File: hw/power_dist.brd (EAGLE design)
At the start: 80 x 50 mm, 87 parts, among them J1 JST-ZH6SMT_VERT, J2 JST-PH4SMT_VERT, J3 JST-PH5VERT, P1 XT30P, P2 XT30P, P3 XT30P, P4 XT30P, P5 XT30P, P6 XT30P, P7 XT90PW-M, Q1 PSMN4R8-100BSEJ, Q2 PSMN4R8-100BSEJ, Q3 PSMN4R8-100BSEJ, Q4 MF-DSC-SOT233-MMBT3904, Q5 MMBT5401 100V, U1 MAX15062AATA+T, U2 STM32G474CEU6, U3 TPS2490DGSR, U4 TCAN334G, U5 LT1787HVIMS8PBF, U6 STLM20DD9FUDFN-4L_STM-L

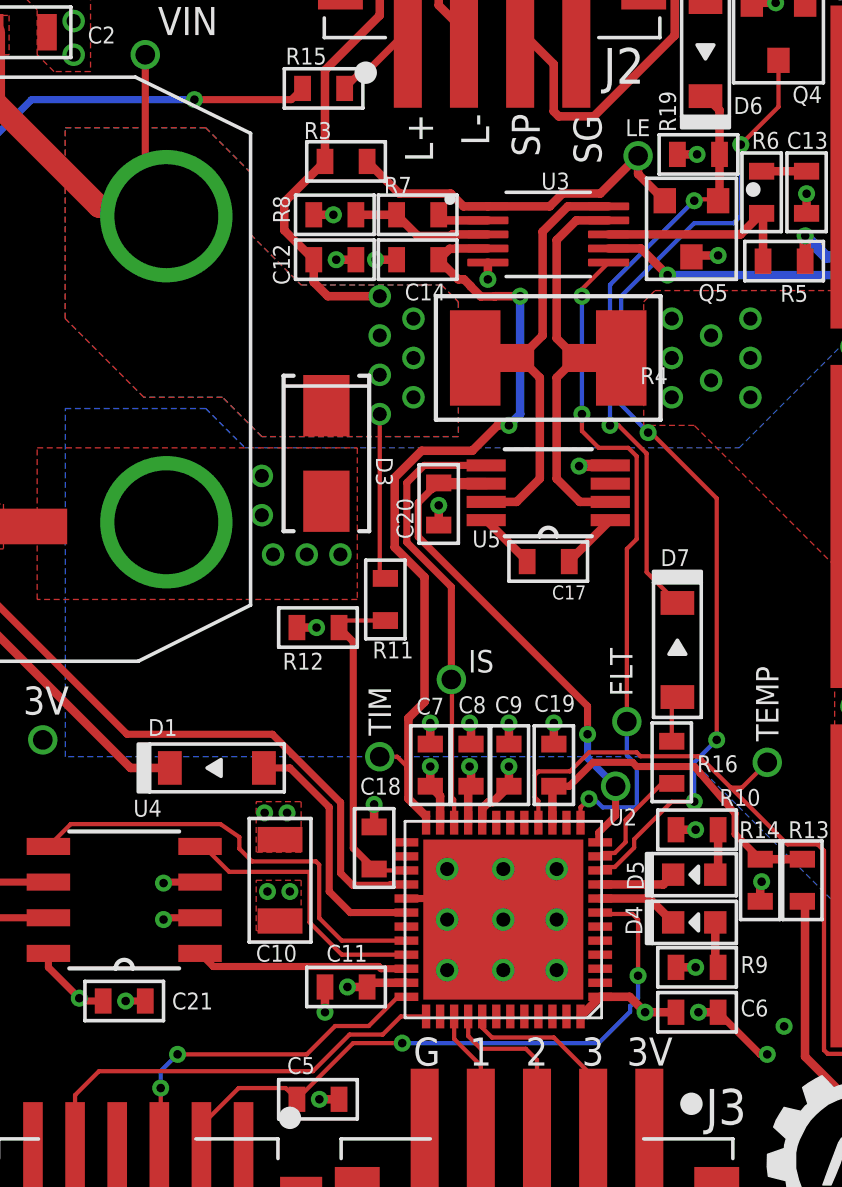
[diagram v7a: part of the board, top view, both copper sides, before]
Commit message: Update version pins for r4.2
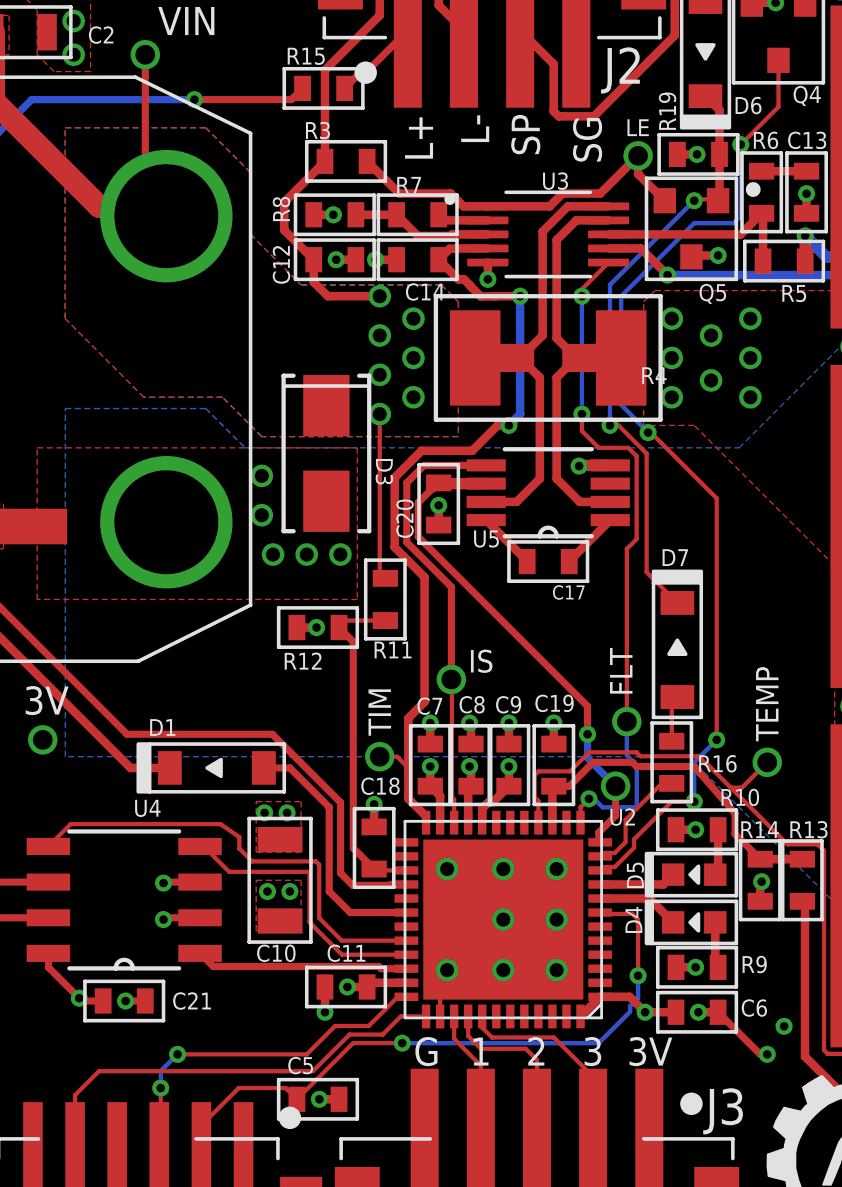
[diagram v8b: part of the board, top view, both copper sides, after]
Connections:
- net GND: now also U2.38; no longer U2.29
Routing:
- net GND: track 64.6 -> 64.5 mm, vias 51 -> 50
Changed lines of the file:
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@@
 <attribute name="HOUSEPART" value="1" x="32.35" y="38.3" size="1.778" layer="27" display="off"/>
 <attribute name="MPN" value="" x="32.35" y="38.3" size="1.778" layer="27" display="off"/>
-<attribute name="NAME" x="31.15" y="39.05" size="0.6" layer="25" font="vector" ratio="10"/>
+<attribute name="NAME" x="31.55" y="39.05" size="0.6" layer="25" font="vector" ratio="10"/>
 <attribute name="POPULATE" value="1" x="32.35" y="38.3" size="1.778" layer="27" display="off"/>
 <attribute name="TOLERANCE" value="" x="32.35" y="38.3" size="1.778" layer="27" display="off"/>
@@
 <contactref element="C2" pad="P$2"/>
 <contactref element="J3" pad="5"/>
-<contactref element="U2" pad="29"/>
 <contactref element="DB_G" pad="P$1"/>
 <via x="20.1" y="45.2" extent="1-16" drill="0.5"/>
@@
 <via x="35.4" y="15" extent="1-16" drill="0.5"/>
 <via x="37.3" y="15" extent="1-16" drill="0.5"/>
-<via x="33.4" y="13.2" extent="1-16" drill="0.5"/>
 <via x="35.4" y="13.2" extent="1-16" drill="0.5"/>
 <via x="37.3" y="13.2" extent="1-16" drill="0.5"/>
@@
 <via x="35.4" y="11.4" extent="1-16" drill="0.5"/>
 <via x="33.4" y="11.4" extent="1-16" drill="0.5"/>
-<wire x1="31.95" y1="13.95" x2="32.65" y2="13.95" width="0.254" layer="1"/>
-<wire x1="32.65" y1="13.95" x2="33.4" y2="13.2" width="0.254" layer="1"/>
 <wire x1="32.6" y1="5.14" x2="32.67" y2="5.07" width="0.254" layer="1"/>
 <via x="10" y="16.8" extent="1-16" drill="0.3048"/>
@@
 <wire x1="44.8" y1="8.4" x2="44.55" y2="8.4" width="0.254" layer="1"/>
 <wire x1="44.55" y1="8.4" x2="43.05" y2="9.9" width="0.254" layer="1"/>
+<contactref element="U2" pad="38"/>
+<wire x1="33.15" y1="9.75" x2="33.15" y2="11.15" width="0.1524" layer="1"/>
+<wire x1="33.15" y1="11.15" x2="33.4" y2="11.4" width="0.1524" layer="1"/>
+<wire x1="42.3" y1="40.45" x2="44.25" y2="45.8" width="0" layer="19" extent="1-1"/>
+<wire x1="42.1" y1="36.8" x2="42.3" y2="40.45" width="0" layer="19" extent="1-1"/>
+<wire x1="46.2" y1="38.35" x2="43.05" y2="36.85" width="0" layer="19" extent="1-1"/>
+<wire x1="34.85" y1="36.6" x2="42.1" y2="36.8" width="0" layer="19" extent="1-1"/>
+<wire x1="31.6" y1="36.7" x2="34.85" y2="36.6" width="0" layer="19" extent="1-1"/>
+<wire x1="30.15" y1="36.7" x2="30.85" y2="36.7" width="0" layer="19" extent="1-1"/>
+<wire x1="29.35" y1="38.3" x2="29.45" y2="36.7" width="0" layer="19" extent="1-1"/>
+<wire x1="38.1" y1="29.35" x2="34.85" y2="36" width="0" layer="19" extent="1-1"/>
+<wire x1="33.1" y1="27.95" x2="38.1" y2="29.35" width="0" layer="19" extent="1-1"/>
+<wire x1="28.75" y1="23.6" x2="33.1" y2="27.25" width="0" layer="19" extent="1-1"/>
+<wire x1="32.8" y1="20.2" x2="28.75" y2="23.6" width="0" layer="19" extent="1-1"/>
+<wire x1="34.2" y1="20.2" x2="32.8" y2="20.2" width="0" layer="19" extent="1-1"/>
+<wire x1="35.6" y1="19.45" x2="34.25" y2="19.45" width="0" layer="19" extent="1-1"/>
+<wire x1="37.2" y1="19.45" x2="35.6" y2="19.45" width="0" layer="19" extent="1-1"/>
+<wire x1="30.8" y1="17.3" x2="32.8" y2="19.45" width="0" layer="19" extent="1-1"/>
+<wire x1="33.4" y1="15" x2="30.8" y2="16.5" width="0" layer="19" extent="1-1"/>
+<wire x1="35.4" y1="15" x2="33.4" y2="15" width="0" layer="19" extent="1-1"/>
+<wire x1="35.4" y1="13.2" x2="35.4" y2="15" width="0" layer="19" extent="1-1"/>
+<wire x1="35.4" y1="11.4" x2="35.4" y2="13.2" width="0" layer="19" extent="1-1"/>
+<wire x1="37.3" y1="15" x2="35.4" y2="15" width="0" layer="19" extent="1-1"/>
+<wire x1="37.3" y1="13.2" x2="37.3" y2="15" width="0" layer="19" extent="1-1"/>
+<wire x1="37.3" y1="11.4" x2="37.3" y2="13.2" width="0" layer="19" extent="1-1"/>
+<wire x1="33.4" y1="11.4" x2="35.4" y2="11.4" width="0" layer="19" extent="1-1"/>
+<wire x1="27.7" y1="17" x2="30.8" y2="17.3" width="0" layer="19" extent="1-1"/>
+<wire x1="26.9" y1="17" x2="27.7" y2="17" width="0" layer="19" extent="1-1"/>
+<wire x1="27.45" y1="16.05" x2="27.7" y2="17" width="0" layer="19" extent="1-1"/>
+<wire x1="24.6" y1="13.265" x2="27.45" y2="16.05" width="0" layer="19" extent="1-1"/>
+<wire x1="21.15" y1="10.3" x2="23.3" y2="13.2" width="0" layer="19" extent="1-1"/>
+<wire x1="29.05" y1="9.9" x2="33.15" y2="9.75" width="0" layer="19" extent="1-1"/>
+<wire x1="28.85" y1="6.8" x2="29.05" y2="9.9" width="0" layer="19" extent="1-1"/>
+<wire x1="32.6" y1="5.14" x2="29.55" y2="6.8" width="0" layer="19" extent="1-1"/>
+<wire x1="42.35" y1="9.9" x2="37.3" y2="11.4" width="0" layer="19" extent="1-1"/>
+<wire x1="44.55" y1="13.85" x2="43.05" y2="9.9" width="0" layer="19" extent="1-1"/>
+<wire x1="21.65" y1="4.6" x2="21.15" y2="10.3" width="0" layer="19" extent="1-1"/>
+<wire x1="14.54" y1="16.8" x2="19.2" y2="11.995" width="0" layer="19" extent="1-1"/>
+<wire x1="16.6" y1="19.6" x2="14.54" y2="16.8" width="0" layer="19" extent="1-1"/>
+<wire x1="16.9" y1="26.8" x2="16.6" y2="19.6" width="0" layer="19" extent="1-1"/>
+<wire x1="16.9" y1="27.6" x2="16.9" y2="26.8" width="0" layer="19" extent="1-1"/>
+<wire x1="17.965" y1="27.2" x2="16.9" y2="26.8" width="0" layer="19" extent="1-1"/>
+<wire x1="8.8" y1="9.1" x2="10" y2="16.8" width="0" layer="19" extent="1-1"/>
+<wire x1="34" y1="44.86" x2="29.35" y2="38.3" width="0" layer="19" extent="1-1"/>
+<wire x1="20.1" y1="44" x2="28.65" y2="38.3" width="0" layer="19" extent="1-1"/>
+<wire x1="20.1" y1="45.2" x2="20.1" y2="44" width="0" layer="19" extent="1-1"/>
+<wire x1="19.15" y1="44.8" x2="20.1" y2="45.2" width="0" layer="19" extent="1-1"/>
+<wire x1="19.8" y1="46.4" x2="20.1" y2="45.2" width="0" layer="19" extent="1-1"/>
+<wire x1="19.8" y1="47.6" x2="19.8" y2="46.4" width="0" layer="19" extent="1-1"/>
+<wire x1="18.55" y1="47" x2="19.8" y2="46.4" width="0" layer="19" extent="1-1"/>
+<wire x1="14.8" y1="47.8" x2="18.55" y2="47" width="0" layer="19" extent="1-1"/>
+<wire x1="12.65" y1="49" x2="14.8" y2="47.8" width="0" layer="19" extent="1-1"/>
+<wire x1="8" y1="48.65" x2="11.85" y2="49" width="0" layer="19" extent="1-1"/>
+<wire x1="7.6" y1="47.6" x2="8" y2="48.65" width="0" layer="19" extent="1-1"/>
+<wire x1="6.4" y1="48" x2="7.6" y2="47.6" width="0" layer="19" extent="1-1"/>
+<wire x1="6.4" y1="49" x2="6.4" y2="48" width="0" layer="19" extent="1-1"/>
 </signal>
 <signal name="VCC" class="1">
